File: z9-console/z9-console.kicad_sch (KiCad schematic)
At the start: 4 parts

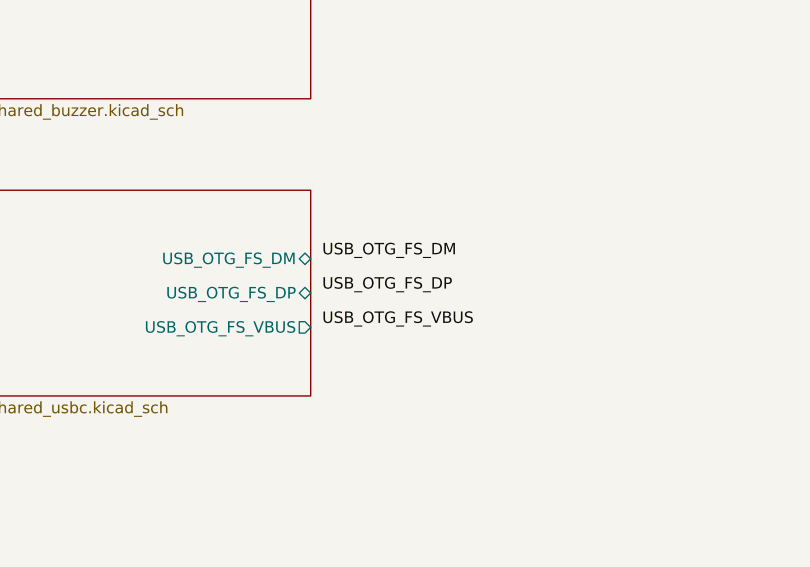
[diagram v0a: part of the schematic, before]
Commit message: Update reference designators and adjust USB label positions for consistency
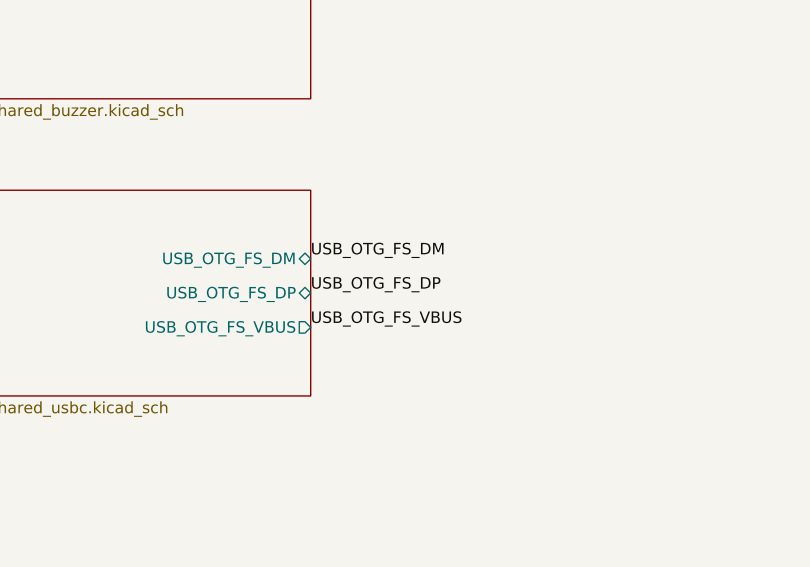
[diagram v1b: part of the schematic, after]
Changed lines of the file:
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@@
 	)
 	(label "USB_OTG_FS_DP"
-		(at 351.79 97.79 0)
+		(at 350.52 97.79 0)
 		(effects
 			(font
@@
 	)
 	(label "USB_OTG_FS_VBUS"
-		(at 351.79 101.6 0)
+		(at 350.52 101.6 0)
 		(effects
 			(font
@@
 	)
 	(label "USB_OTG_FS_DM"
-		(at 351.79 93.98 0)
-		(effects
-			(font
+		(at 350.52 93.98 0)
+		(effects
+			(font

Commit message: x
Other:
- added sheet shared_esp32 (../z9-shared/shared_usbc_esp32.kicad_sch)
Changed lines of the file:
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@@
+	)
+	(sheet
+		(at 53.34 129.54)
+		(size 41.91 24.13)
+		(exclude_from_sim no)
+		(in_bom yes)
+		(on_board yes)
+		(dnp no)
+		(fields_autoplaced yes)
+		(stroke
+			(width 0.1524)
+			(type solid)
+		)
+		(fill
+			(color 0 0 0 0.0000)
+		)
+		(property "Sheetname" "shared_esp32"
+			(at 53.34 128.8284 0)
+			(effects
+				(font
+					(size 1.27 1.27)
+				)
+				(justify left bottom)
+			)
+		)
+		(property "Sheetfile" "../z9-shared/shared_usbc_esp32.kicad_sch"
+			(at 53.34 154.2546 0)
+			(effects
+				(font
+					(size 1.27 1.27)
+				)
+				(justify left top)
+			)
+		)
+		(instances
+			(project "z9-console"
+				(path "/8d063f79-9282-4820-bcf4-1ff3c006cf08"
+					(page "825")
+				)
+			)
+		)
 	)
 	(sheet

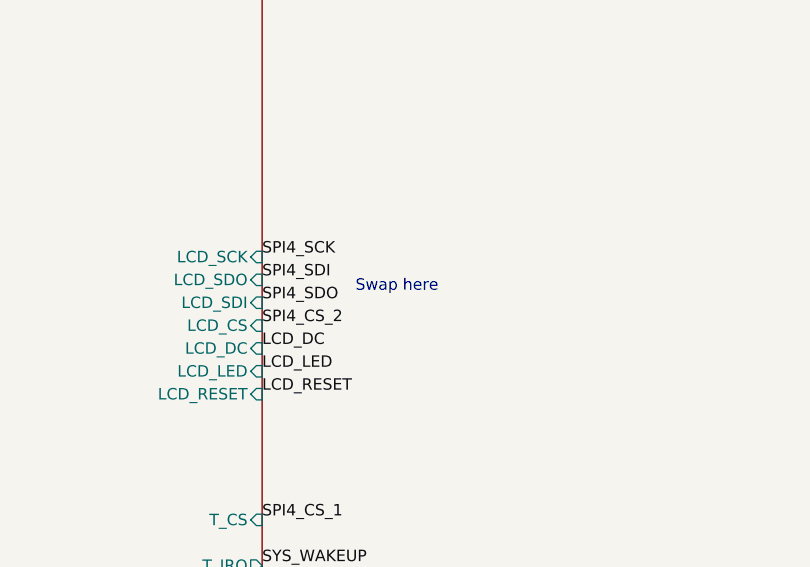
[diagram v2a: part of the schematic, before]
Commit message: Update KiCad project and schematic files for z9-console - Changed project UUID in z9-console.kicad_pro to a new unique identifier. - Updated schematic version from 20250114 to 20260306 and generator version from 9.0 to 10.0 in z9-console.kicad_sch. - Modified date in title block to 2026-04-29. - Added properties for components to control visibility and autoplace behavior. - Ensured all mounting holes have consistent properties for reference, value, footprint, and description. - Updated project references in instances to match the new project name. - Cleaned up color properties in fill elements to ensure proper rendering.
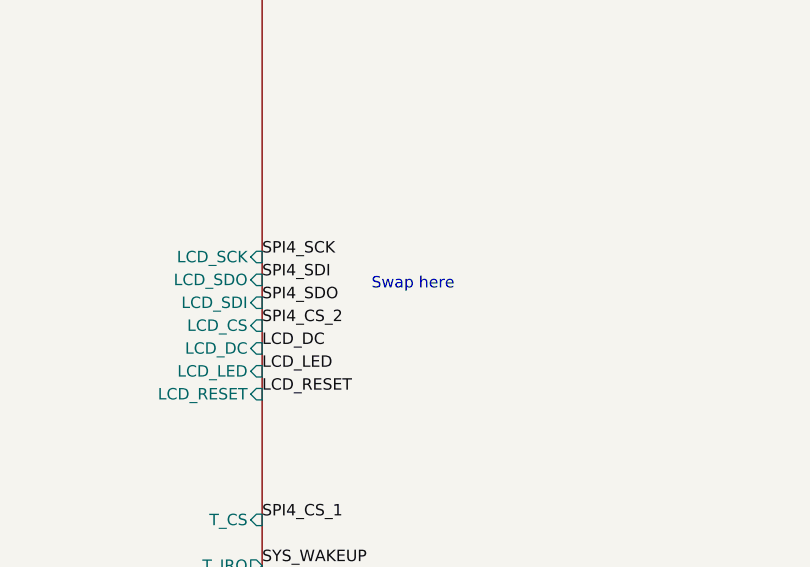
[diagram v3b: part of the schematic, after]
